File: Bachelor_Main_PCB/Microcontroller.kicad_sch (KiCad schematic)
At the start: 7 parts, among them U3 STM32H7A3ZITxQ, U4 USB3320C-EZK-TR, Y1 SG-210STF 24Mhz

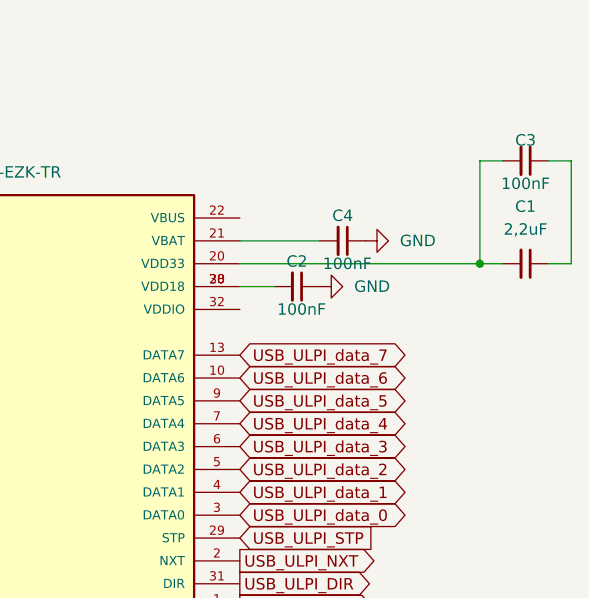
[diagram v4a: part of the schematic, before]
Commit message: Add more bypass caps
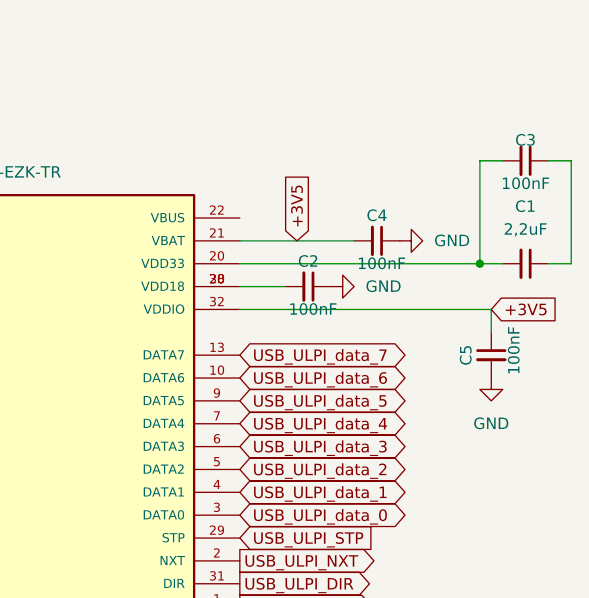
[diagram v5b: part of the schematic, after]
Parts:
- added C5: 100nF, Capacitor_SMD:C_0603_1608Metric, symbol Device:C_Small
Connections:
- net GND: now also C5.2
- net +3V5: now reaches C4.2, U4.21 (VBAT)
- net +3V5: now also U4.32 (VDDIO), C5.1
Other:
- moved on the sheet: C2, C4

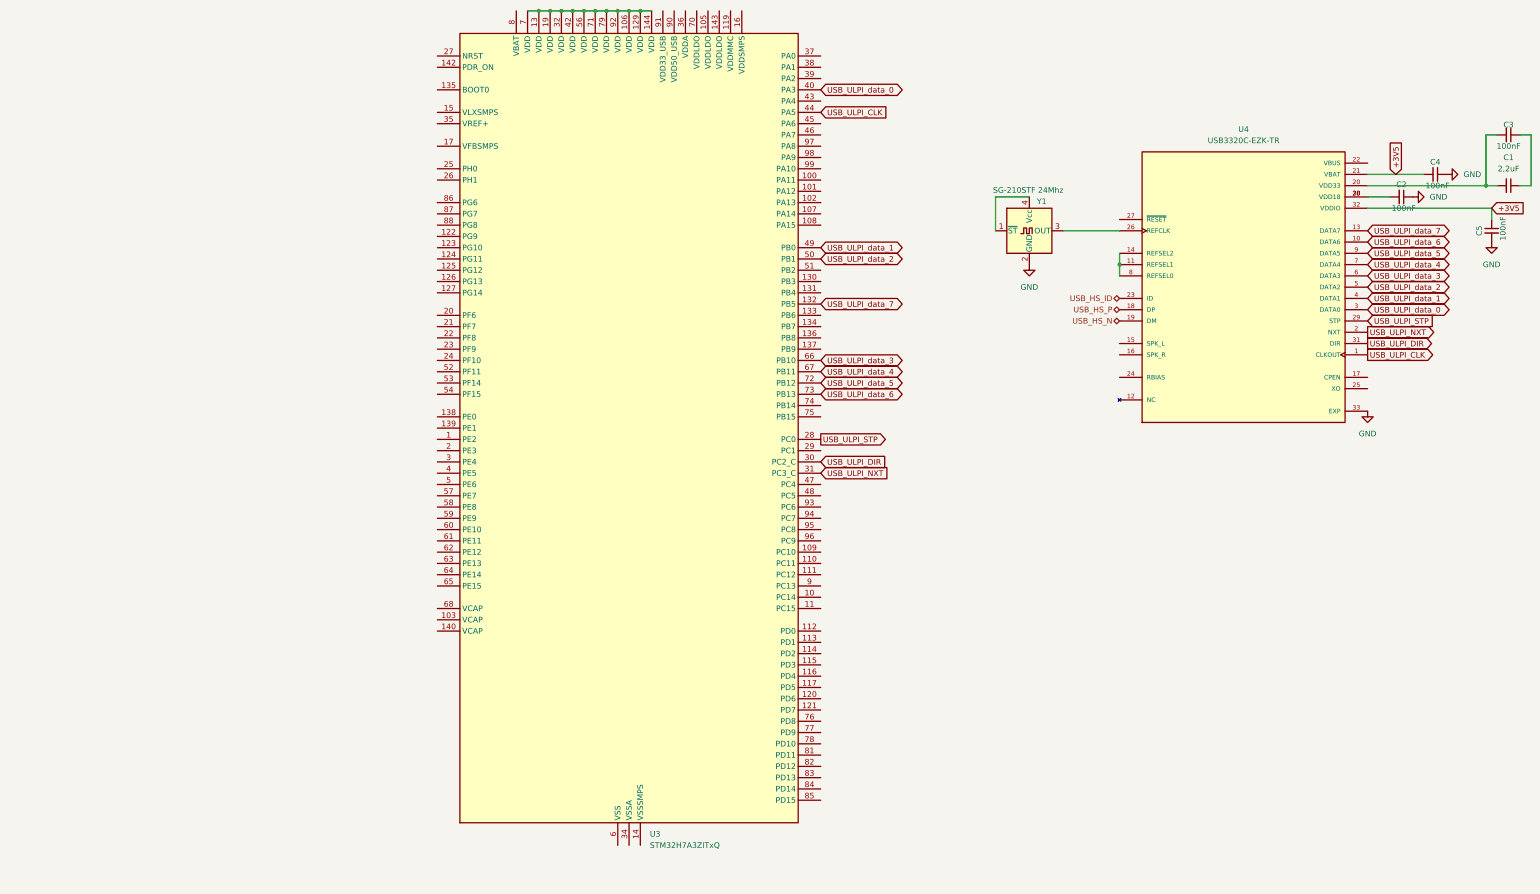
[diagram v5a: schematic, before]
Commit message: Fix bypass cap routing
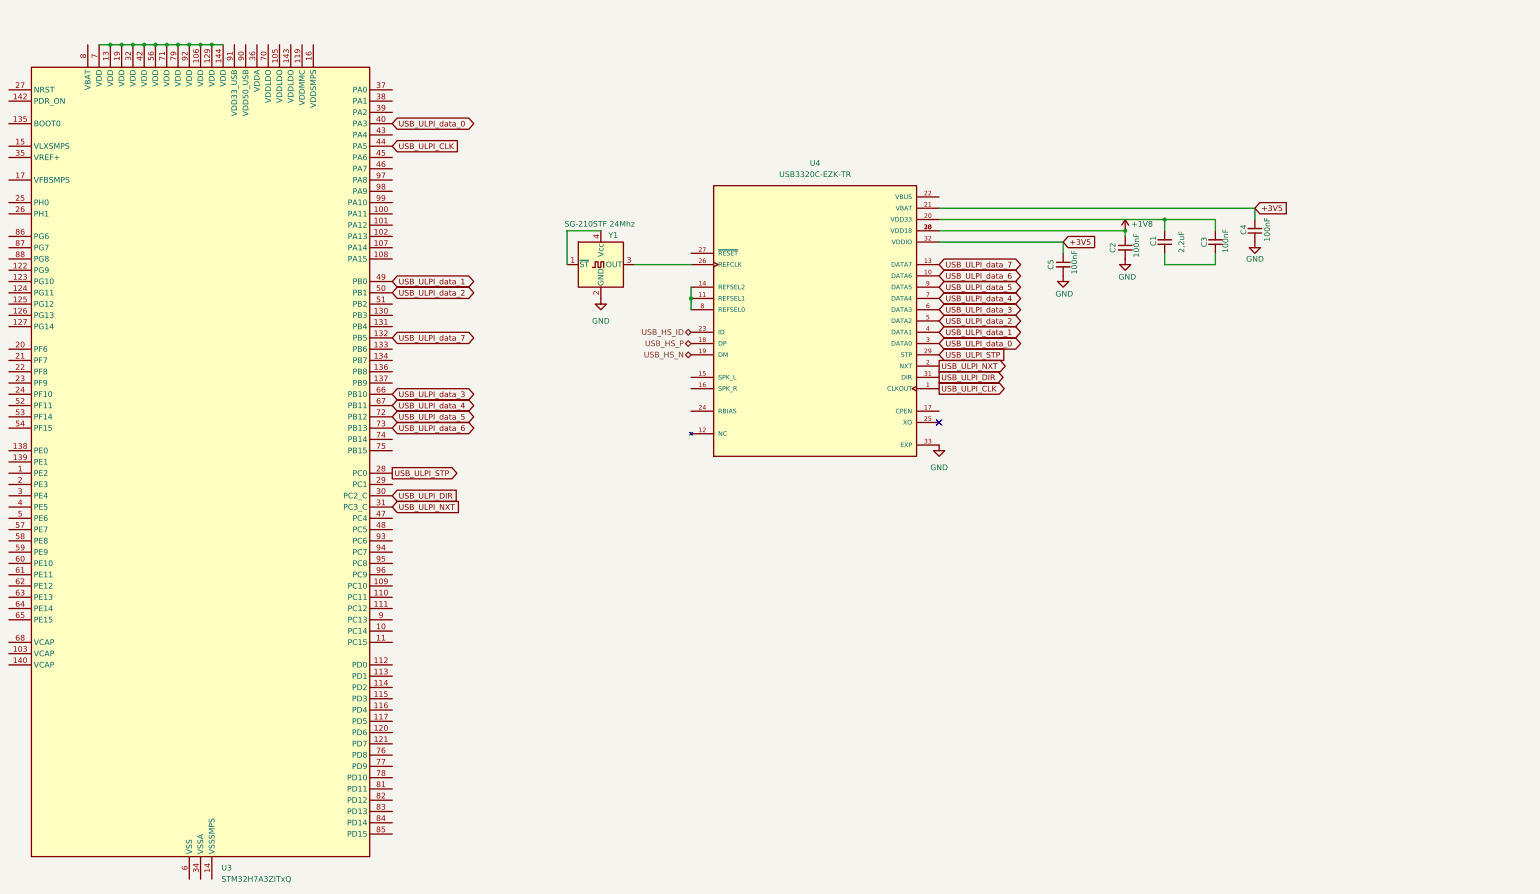
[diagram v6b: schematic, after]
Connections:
- net GND: now also C2.2; no longer C2.1
- net +1V8: now reaches U4.28 (VDD18), U4.30 (VDD18)
- net +1V8: now also C2.1; no longer C2.2
- no-connect marks 0 -> 1
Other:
- moved on the sheet: C1, C2, C3, C4, C5, U3, U4, Y1

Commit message: Add Rbias resisstor to USB3320
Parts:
- added R2: 8k06, Resistor_SMD:R_0201_0603Metric_Pad0.64x0.40mm_HandSolder, symbol Device:R_Small
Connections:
- net +3V5: now also U4.11 (REFSEL1), U4.14 (REFSEL2), U4.8 (REFSEL0)
- net GND: now also R2.2
- net at U4.24 (RBIAS): now also R2.1
- no-connect marks 1 -> 3
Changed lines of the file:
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@@
+	)
+	(no_connect
+		(at 210.82 130.81)
+	)
+	(no_connect
+		(at 210.82 133.35)
 	)
 	(no_connect
@@
 	(wire
 		(pts
+			(xy 210.82 113.03) (xy 210.82 110.49)
+		)
+		(stroke
+			(width 0)
+			(type default)
+		)
+	)
+	(wire
+		(pts
 			(xy 328.93 95.25) (xy 328.93 97.79)
 		)
@@
 	(wire
 		(pts
+			(xy 198.12 138.43) (xy 210.82 138.43)
+		)
+		(stroke
+			(width 0)
+			(type default)
+		)
+	)
+	(wire
+		(pts
 			(xy 90.17 55.88) (xy 92.71 55.88)
 		)
@@
 		(pts
 			(xy 100.33 55.88) (xy 102.87 55.88)
-		)
-		(stroke
-			(width 0)
-			(type default)
-		)
-	)
-	(wire
-		(pts
-			(xy 210.82 110.49) (xy 210.82 113.03)
 		)
 		(stroke
@@
 				)
 				(justify left)
+				(hide yes)
+			)
+		)
+	)
+	(global_label "+3V5"
+		(shape input)
+		(at 210.82 113.03 180)
+		(fields_autoplaced yes)
+		(effects
+			(font
+				(size 1.27 1.27)
+			)
+			(justify right)
+		)
+		(property "Intersheetrefs" "${INTERSHEET_REFS}"
+			(at 202.7548 113.03 0)
+			(effects
+				(font
+					(size 1.27 1.27)
+				)
+				(justify right)
 				(hide yes)
 			)
@@
 	)
 	(symbol
+		(lib_id "power:GND")
+		(at 198.12 143.51 0)
+		(unit 1)
+		(exclude_from_sim no)
+		(in_bom yes)
+		(on_board yes)
+		(dnp no)
+		(fields_autoplaced yes)
+		(property "Reference" "#PWR011"
+			(at 198.12 149.86 0)
+			(effects
+				(font
+					(size 1.27 1.27)
+				)
+				(hide yes)
+			)
+		)
+		(property "Value" "GND"
+			(at 198.12 148.59 0)
+			(effects
+				(font
+					(size 1.27 1.27)
+				)
+			)
+		)
+		(property "Footprint" ""
+			(at 198.12 143.51 0)
+			(effects
+				(font
+					(size 1.27 1.27)
+				)
+				(hide yes)
+			)
+		)
+		(property "Datasheet" ""
+			(at 198.12 143.51 0)
+			(effects
+				(font
+					(size 1.27 1.27)
+				)
+				(hide yes)
+			)
+		)
+		(property "Description" "Power symbol creates a global label with name \"GND\" , ground"
+			(at 198.12 143.51 0)
+			(effects
+				(font
+					(size 1.27 1.27)
+				)
+				(hide yes)
+			)
+		)
+		(pin "1"
+		)
+		(instances
+			(project "Bachelor_Main_PCB"
+				(path "/3544d663-329e-4884-b753-28436ca187e8/9cdc091d-5c59-45ee-8211-bdd0f330a333"
+					(reference "#PWR011")
+					(unit 1)
+				)
+			)
+		)
+	)
+	(symbol
 		(lib_id "Device:C_Small")
 		(at 294.64 105.41 0)
@@
 					(unit 1)
 				)
+			)
+		)
+	)
+	(symbol
+		(lib_id "Device:R_Small")
+		(at 198.12 140.97 0)
+		(unit 1)
+		(exclude_from_sim no)
+		(in_bom yes)
+		(on_board yes)
+		(dnp no)
+		(fields_autoplaced yes)
+		(property "Reference" "R2"
+			(at 200.66 139.6999 0)
+			(effects
+				(font
+					(size 1.27 1.27)
+				)
+				(justify left)
+			)
+		)
+		(property "Value" "8k06"
+			(at 200.66 142.2399 0)
+			(effects
+				(font
+					(size 1.27 1.27)
+				)
+				(justify left)
+			)
+		)
+		(property "Footprint" "Resistor_SMD:R_0201_0603Metric_Pad0.64x0.40mm_HandSolder"
+			(at 198.12 140.97 0)
+			(effects
+				(font
+					(size 1.27 1.27)
+				)
+				(hide yes)
+			)
+		)
+		(property "Datasheet" "~"
+			(at 198.12 140.97 0)
+			(effects
+				(font
+					(size 1.27 1.27)
+				)
+				(hide yes)
+			)
+		)
+		(property "Description" "Resistor, small symbol"
+			(at 198.12 140.97 0)
+			(effects
+				(font
+					(size 1.27 1.27)
+				)
+				(hide yes)
+			)
+		)
+		(pin "1"
+		)
+		(pin "2"
+		)
+		(instances
+			(project ""
+				(path "/3544d663-329e-4884-b753-28436ca187e8/9cdc091d-5c59-45ee-8211-bdd0f330a333"
+					(reference "R2")
+					(unit 1)
+				)

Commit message: Route ID pin on USB3320, Fix 0603 footprint on resistors
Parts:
- added R3: 10k, Resistor_SMD:R_0603_1608Metric_Pad0.98x0.95mm_HandSolder, symbol Device:R_Small
- R2: footprint Resistor_SMD:R_0201_0603Metric_Pad0.64x0.40mm_HandSolder -> Resistor_SMD:R_0603_1608Metric_Pad0.98x0.95mm_HandSolder
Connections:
- net USB_HS_ID is gone; now on an unnamed net: U4.23 (ID)
- net at U4.22 (VBUS): now also R3.1
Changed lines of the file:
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@@
+	)
+	(junction
+		(at 273.05 95.25)
+		(diameter 0)
+		(color 0 0 0 0)
 	)
 	(junction
@@
 	(wire
 		(pts
+			(xy 210.82 120.65) (xy 200.66 120.65)
+		)
+		(stroke
+			(width 0)
+			(type default)
+		)
+	)
+	(wire
+		(pts
 			(xy 102.87 55.88) (xy 105.41 55.88)
 		)
@@
 	(wire
 		(pts
-			(xy 266.7 95.25) (xy 317.5 95.25)
+			(xy 273.05 95.25) (xy 317.5 95.25)
+		)
+		(stroke
+			(width 0)
+			(type default)
+		)
+	)
+	(wire
+		(pts
+			(xy 266.7 95.25) (xy 273.05 95.25)
 		)
 		(stroke
@@
 	(wire
 		(pts
+			(xy 266.7 90.17) (xy 279.4 90.17)
+		)
+		(stroke
+			(width 0)
+			(type default)
+		)
+	)
+	(wire
+		(pts
+			(xy 200.66 81.28) (xy 200.66 120.65)
+		)
+		(stroke
+			(width 0)
+			(type default)
+		)
+	)
+	(wire
+		(pts
 			(xy 337.82 95.25) (xy 337.82 92.71)
 		)
@@
 	(wire
 		(pts
+			(xy 200.66 81.28) (xy 273.05 81.28)
+		)
+		(stroke
+			(width 0)
+			(type default)
+		)
+	)
+	(wire
+		(pts
 			(xy 80.01 55.88) (xy 82.55 55.88)
 		)
@@
 		(pts
 			(xy 82.55 55.88) (xy 85.09 55.88)
+		)
+		(stroke
+			(width 0)
+			(type default)
+		)
+	)
+	(wire
+		(pts
+			(xy 273.05 81.28) (xy 273.05 95.25)
 		)
 		(stroke
@@
 		(shape bidirectional)
 		(at 210.82 125.73 180)
-		(effects
-			(font
-				(size 1.27 1.27)
-			)
-			(justify right)
-		)
-	)
-	(hierarchical_label "USB_HS_ID"
-		(shape bidirectional)
-		(at 210.82 120.65 180)
 		(effects
 			(font
@@
 			)
 		)
-		(property "Footprint" "Resistor_SMD:R_0201_0603Metric_Pad0.64x0.40mm_HandSolder"
+		(property "Footprint" "Resistor_SMD:R_0603_1608Metric_Pad0.98x0.95mm_HandSolder"
 			(at 198.12 140.97 0)
 			(effects
@@
 					(unit 1)
 				)
+			)
+		)
+	)
+	(symbol
+		(lib_id "Device:R_Small")
+		(at 281.94 90.17 90)
+		(unit 1)
+		(exclude_from_sim no)
+		(in_bom yes)
+		(on_board yes)
+		(dnp no)
+		(fields_autoplaced yes)
+		(property "Reference" "R3"
+			(at 281.94 85.09 90)
+			(effects
+				(font
+					(size 1.27 1.27)
+				)
+			)
+		)
+		(property "Value" "10k"
+			(at 281.94 87.63 90)
+			(effects
+				(font
+					(size 1.27 1.27)
+				)
+			)
+		)
+		(property "Footprint" "Resistor_SMD:R_0603_1608Metric_Pad0.98x0.95mm_HandSolder"
+			(at 281.94 90.17 0)
+			(effects
+				(font
+					(size 1.27 1.27)
+				)
+				(hide yes)
+			)
+		)
+		(property "Datasheet" "~"
+			(at 281.94 90.17 0)
+			(effects
+				(font
+					(size 1.27 1.27)
+				)
+				(hide yes)
+			)
+		)
+		(property "Description" "Resistor, small symbol"
+			(at 281.94 90.17 0)
+			(effects
+				(font
+					(size 1.27 1.27)
+				)
+				(hide yes)
+			)
+		)
+		(pin "1"
+		)
+		(pin "2"
+		)
+		(instances
+			(project "Bachelor_Main_PCB"
+				(path "/3544d663-329e-4884-b753-28436ca187e8/9cdc091d-5c59-45ee-8211-bdd0f330a333"
+					(reference "R3")
+					(unit 1)
+				)
